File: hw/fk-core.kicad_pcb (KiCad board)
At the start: 2 copper layers, 98.8 x 37 mm, 110 parts, among them J1 RF-SMA-EDGE, J10 S2B-PH-SM4-TB, J11 RF-SMA-EDGE, J4 Conn_01x01, J5 Conn_01x03, J6 Conn_01x05, J7 CONN-HDR-2x5, J9 MICRO-USB, M1 MOUNT_HOLE, M3 MOUNT_HOLE, M4 MOUNT_HOLE, M6 MOUNT_HOLE, M7 MICROSD, Q1 2N7002LT1G, Q2 2N7002LT1G, Q3 2N7002LT1G, Q4 2N7002LT1G, SW1 SPNO, SW2 SPNO, U1 ATWINC1500-MR210PA, U10 FGPMMOPA6H, U11 MAX1704XX, U2 ATSAMD21G18A-AU, U3 RFM95W, U4 24AA02E64, U5 S25FL116K0XMFI041, U6 BQ24074RGTT, U7 PCF8523, U8 MCP1700T-3302E/MB, U9 ISL8541x, Y1 FC-135, Y2 FC-135

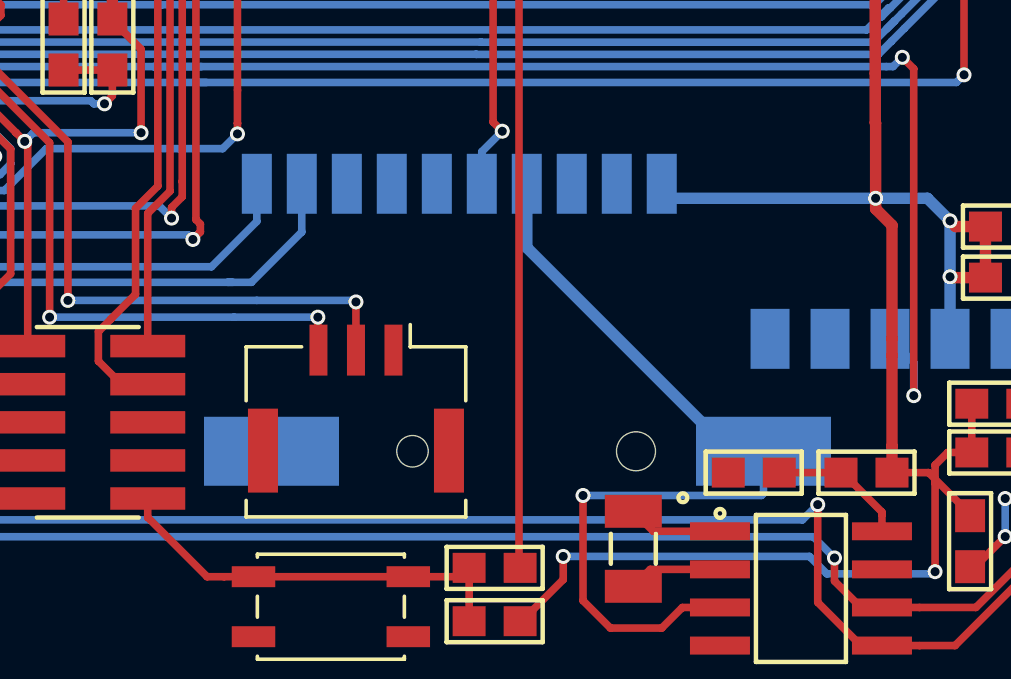
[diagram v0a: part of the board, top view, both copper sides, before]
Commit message: Nudge the coincell away from LoRa.
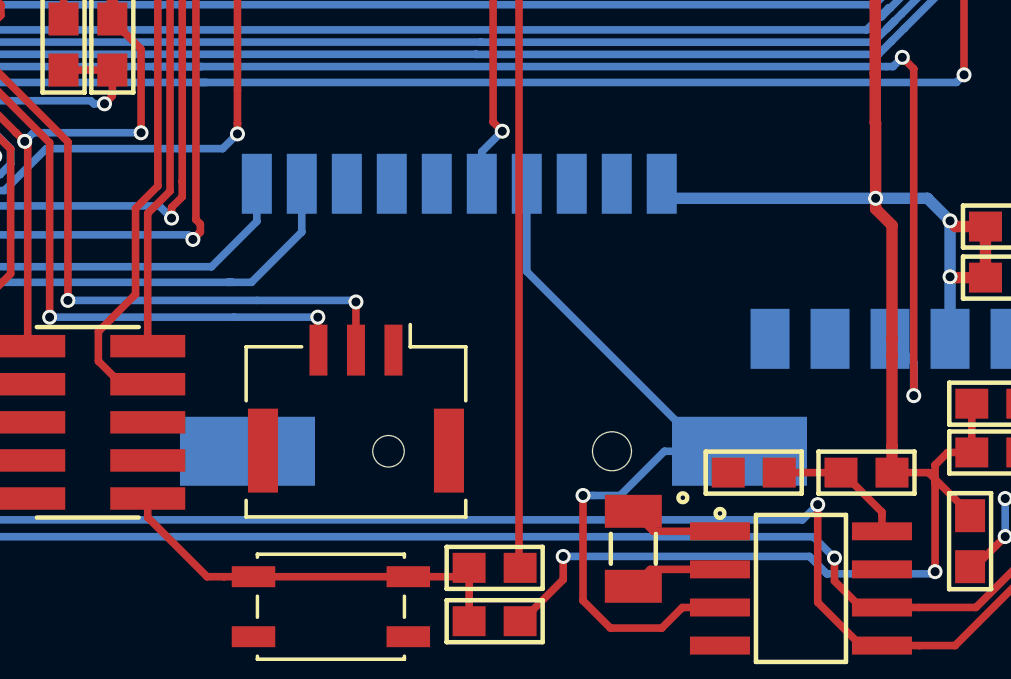
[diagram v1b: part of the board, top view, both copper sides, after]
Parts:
- moved BT1 0.80 mm to (146.3, 139.1)
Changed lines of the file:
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@@
     (links 291)
     (no_connects 0)
-    (area 62.463333 95.834285 186.108401 151.864743)
+    (area 77.293399 109.703799 176.23908 146.887001)
     (thickness 1.6)
     (drawings 23)
-    (tracks 1364)
+    (tracks 1366)
     (zones 0)
     (modules 110)
@@
   )
   (module conservify:BAT_CR1210 (layer B.Cu)
-    (at 147.1168 139.0904 270)
+    (at 146.3168 139.0904 270)
     (fp_text reference BT1 (at 0.15 -12.45 270) (layer B.SilkS) hide
       (effects (font (size 1.5 1.5) (thickness 0.15)) (justify mirror))
@@
   (segment (start 153.3652 114.62) (end 153.3652 113.8768) (width 0.254) (layer F.Cu) (net 32))
   (segment (start 153.3652 113.8768) (end 154.3812 112.8608) (width 0.254) (layer F.Cu) (net 32))
-  (segment (start 149.3012 140.5636) (end 155.2476 140.5636) (width 0.254) (layer B.Cu) (net 34))
-  (segment (start 155.2476 140.5636) (end 155.3168 140.4944) (width 0.254) (layer B.Cu) (net 34))
-  (segment (start 155.3168 140.4944) (end 155.3168 139.0904) (width 0.254) (layer B.Cu) (net 34))
+  (segment (start 147.42668 130.175) (end 147.42668 133.10028) (width 0.254) (layer B.Cu) (net 34))
+  (segment (start 147.42668 133.10028) (end 153.4168 139.0904) (width 0.254) (layer B.Cu) (net 34))
+  (segment (start 153.4168 139.0904) (end 154.5168 139.0904) (width 0.254) (layer B.Cu) (net 34))
+  (segment (start 154.5168 139.0904) (end 152.0128 139.0904) (width 0.254) (layer B.Cu) (net 34))
+  (segment (start 152.0128 139.0904) (end 150.5396 140.5636) (width 0.254) (layer B.Cu) (net 34))
+  (segment (start 150.5396 140.5636) (end 149.654753 140.5636) (width 0.254) (layer B.Cu) (net 34))
+  (segment (start 149.654753 140.5636) (end 149.3012 140.5636) (width 0.254) (layer B.Cu) (net 34))
   (segment (start 151.9258 144.9832) (end 150.213878 144.9832) (width 0.254) (layer F.Cu) (net 34))
   (segment (start 150.213878 144.9832) (end 149.3012 144.070522) (width 0.254) (layer F.Cu) (net 34))
@@
   (segment (start 153.8656 144.2974) (end 152.6116 144.2974) (width 0.254) (layer F.Cu) (net 34))
   (segment (start 152.6116 144.2974) (end 151.9258 144.9832) (width 0.254) (layer F.Cu) (net 34))
-  (segment (start 147.42668 130.6576) (end 147.42668 132.30028) (width 0.381) (layer B.Cu) (net 34))
-  (segment (start 147.42668 132.30028) (end 154.2168 139.0904) (width 0.381) (layer B.Cu) (net 34))
   (segment (start 155.436 139.0904) (end 156.536 139.0904) (width 0.381) (layer B.Cu) (net 34))
   (segment (start 122.102917 117.073717) (end 122.102917 114.946877) (width 0.254) (layer F.Cu) (net 35))
@@
     (connect_pads (clearance 0.2032))
     (min_thickness 0.2032)
-    (fill (arc_segments 32) (thermal_gap 0.254) (thermal_bridge_width 0.254))
+    (fill yes (arc_segments 32) (thermal_gap 0.254) (thermal_bridge_width 0.254))
     (polygon
       (pts
@@
     (connect_pads (clearance 0.2032))
     (min_thickness 0.2032)
-    (fill (arc_segments 32) (thermal_gap 0.254) (thermal_bridge_width 0.254))
+    (fill yes (arc_segments 32) (thermal_gap 0.254) (thermal_bridge_width 0.254))
     (polygon
       (pts
@@
     (connect_pads (clearance 0.2032))
     (min_thickness 0.2032)
-    (fill (arc_segments 32) (thermal_gap 0.254) (thermal_bridge_width 0.254))
+    (fill yes (arc_segments 32) (thermal_gap 0.254) (thermal_bridge_width 0.254))
     (polygon
       (pts
@@
     (connect_pads (clearance 0.2032))
     (min_thickness 0.2032)
-    (fill (arc_segments 32) (thermal_gap 0.254) (thermal_bridge_width 0.254))
+    (fill yes (arc_segments 32) (thermal_gap 0.254) (thermal_bridge_width 0.254))
     (polygon
       (pts
@@
     (connect_pads (clearance 0.2032))
     (min_thickness 0.2032)
-    (fill (arc_segments 32) (thermal_gap 0.254) (thermal_bridge_width 0.254))
+    (fill yes (arc_segments 32) (thermal_gap 0.254) (thermal_bridge_width 0.254))
     (polygon
       (pts
@@
     (connect_pads (clearance 0.2032))
     (min_thickness 0.2032)
-    (fill (arc_segments 32) (thermal_gap 0.254) (thermal_bridge_width 0.254))
+    (fill yes (arc_segments 32) (thermal_gap 0.254) (thermal_bridge_width 0.254))
     (polygon
       (pts
@@
     (connect_pads (clearance 0.2032))
     (min_thickness 0.2032)
-    (fill (arc_segments 32) (thermal_gap 0.254) (thermal_bridge_width 0.254))
+    (fill yes (arc_segments 32) (thermal_gap 0.254) (thermal_bridge_width 0.254))
     (polygon
       (pts
@@
     (connect_pads (clearance 0.2032))
     (min_thickness 0.2032)
-    (fill (arc_segments 32) (thermal_gap 0.254) (thermal_bridge_width 0.254))
+    (fill yes (arc_segments 32) (thermal_gap 0.254) (thermal_bridge_width 0.254))
     (polygon
       (pts

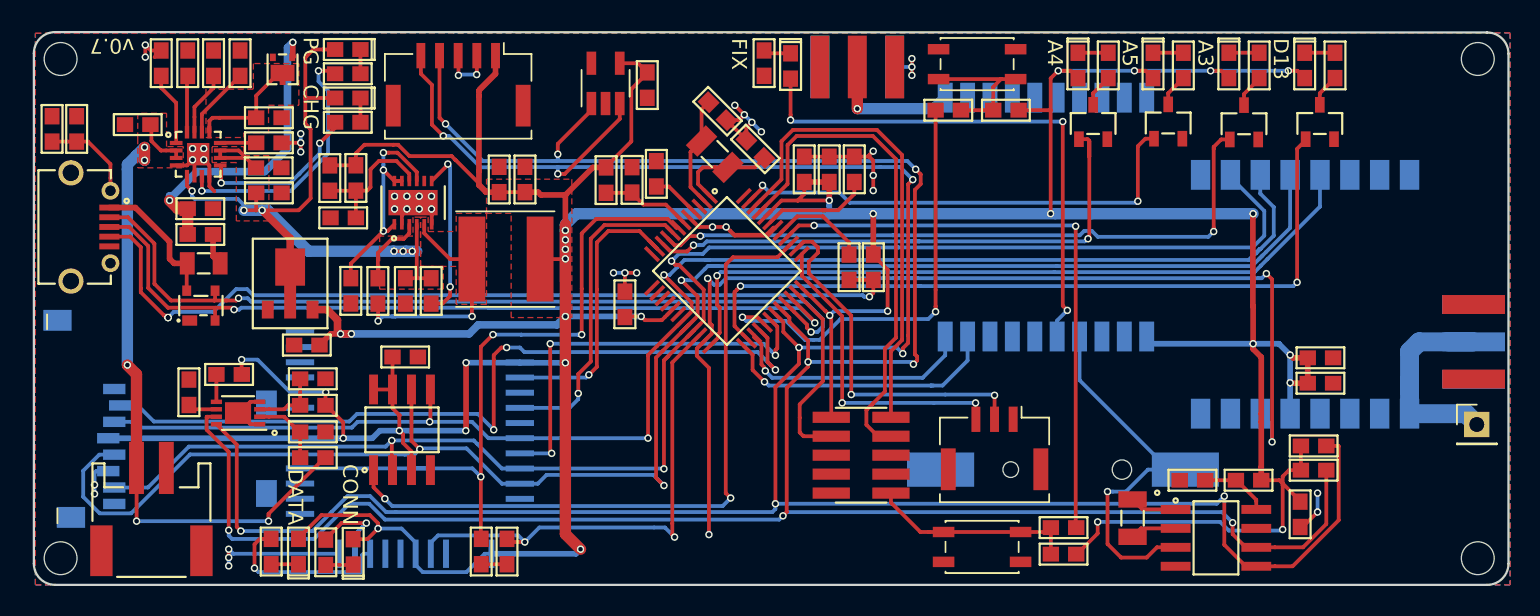
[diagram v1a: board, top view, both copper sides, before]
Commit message: Adding NFET for peripherals.
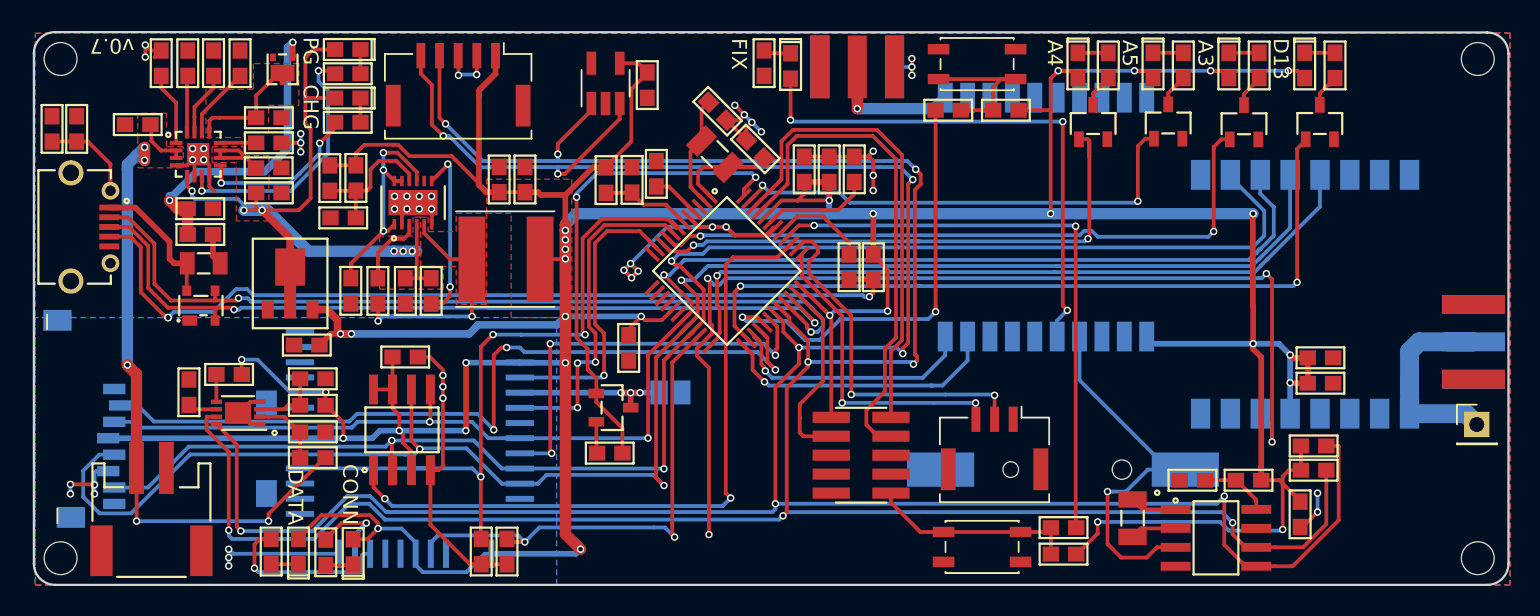
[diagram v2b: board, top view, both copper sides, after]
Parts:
- added J2: Conn_01x02, conservify:SJ_OPEN, B.Cu at (120.0, 133.9)
- added Q5: 2N7002LT1G, RocketScreamKicadLibrary:SOT-23, F.Cu at (116.2, 134.9)
- added R6: 10K, RocketScreamKicadLibrary:RES-0603, F.Cu at (116.0, 138.0)
- moved C5 2.93 mm to (117.2, 130.9), turned to 270 degrees
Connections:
- C18 pad 2: GND -> /PERIPH_GND
- M7 pad 6: GND -> /PERIPH_GND
- M7 pad MT1: GND -> /PERIPH_GND
- M7 pad MT2: GND -> /PERIPH_GND
- R1 pad 2: GND -> /PERIPH_GND
- R2 pad 2: GND -> /PERIPH_GND
- U1 pad 12: GND -> /PERIPH_GND
- U1 pad 28: GND -> /PERIPH_GND
- U1 pad 9: GND -> /PERIPH_GND
- U2 pad 48: Net-(U2-Pad48) -> /PERIPH_EN
- U5 pad 4: GND -> /PERIPH_GND
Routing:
- net /PERIPH_GND: track 0.00 -> 44.5 mm, vias 0 -> 13
- net /PERIPH_EN: track 0.00 -> 32.9 mm, vias 0 -> 2
- net GND: track 84.8 -> 82.7 mm, vias 41 -> 37
- net /WIFI_IRQ: track 22.1 -> 23.5 mm, vias 1 -> 3
- net /WIFI_WAKE: track 19.4 -> 20.6 mm
- added copper zone on B.Cu, net /PERIPH_GND

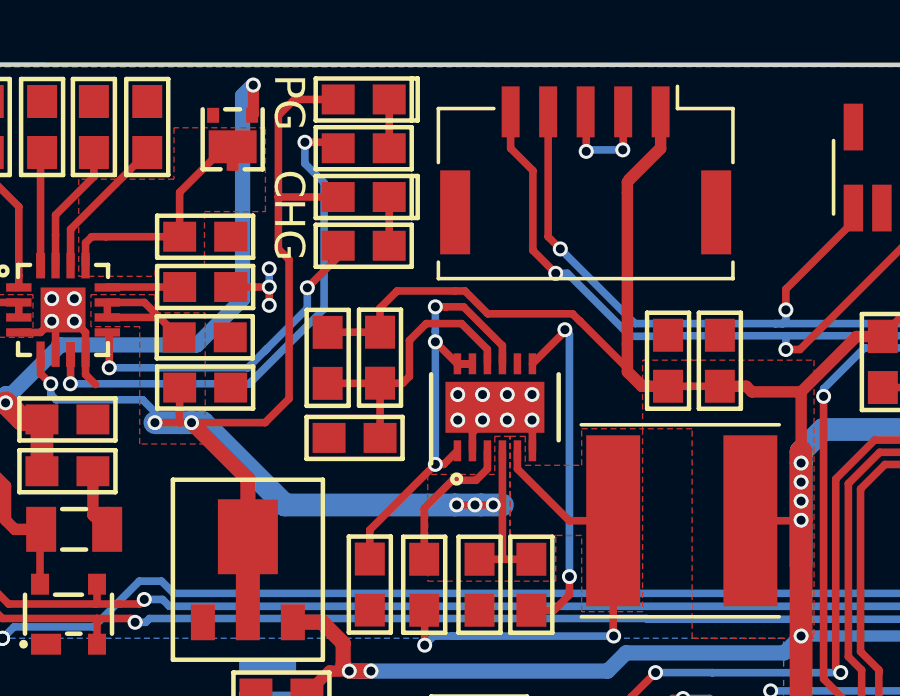
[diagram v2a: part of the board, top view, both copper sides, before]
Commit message: Expose Vbus on the module connector.
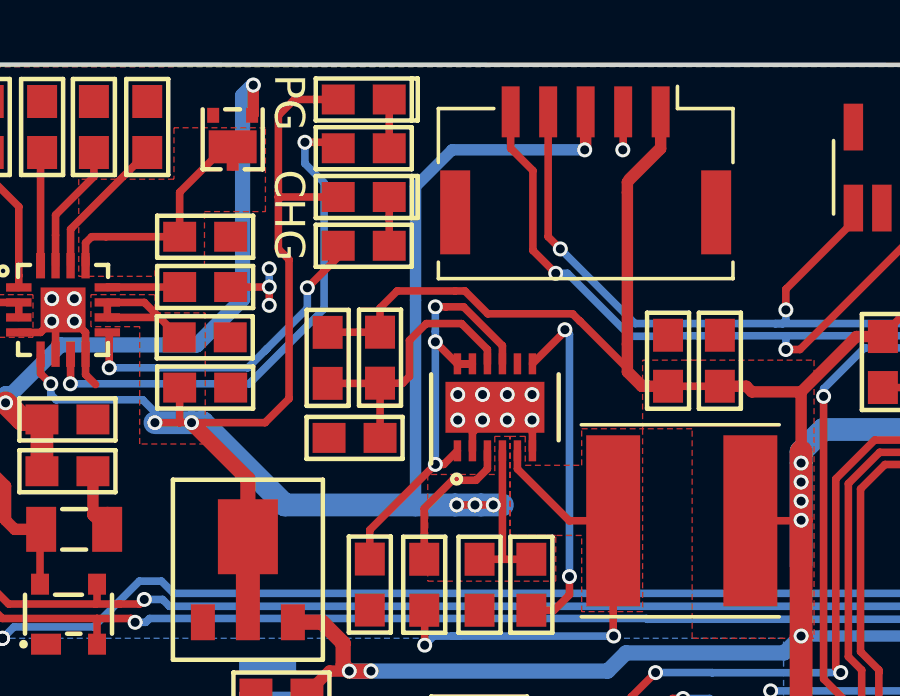
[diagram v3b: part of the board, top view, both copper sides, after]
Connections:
- J6 pad 3: GND -> VBUS
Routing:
- net VBUS: track 57.2 -> 75.3 mm, vias 6 -> 7
- net GND: track 82.7 -> 80.1 mm, vias 37 -> 36
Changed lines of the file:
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@@
     (thickness 1.6)
     (drawings 23)
-    (tracks 1428)
+    (tracks 1432)
     (zones 0)
     (modules 113)
@@
   )
   (setup
-    (last_trace_width 0.254)
+    (last_trace_width 0.381)
     (user_trace_width 0.2032)
     (user_trace_width 0.254)
@@
       (net 1 GND))
     (pad 3 smd rect (at 0 1.95 180) (size 0.6 1.7) (layers F.Cu F.Paste F.Mask)
-      (net 1 GND))
+      (net 42 VBUS))
     (pad 4 smd rect (at 1.25 1.95 180) (size 0.6 1.7) (layers F.Cu F.Paste F.Mask)
       (net 7 /SCL))
@@
   (segment (start 135.0372 112.1156) (end 136.1948 112.1156) (width 0.254) (layer B.Cu) (net 1))
   (via (at 136.1948 112.1156) (size 0.5) (drill 0.3) (layers F.Cu B.Cu) (net 1))
-  (segment (start 105.8164 112.6744) (end 105.8164 111.3752) (width 0.254) (layer F.Cu) (net 1))
-  (segment (start 105.8164 111.3752) (end 105.7976 111.3564) (width 0.254) (layer F.Cu) (net 1))
-  (segment (start 107.0356 112.6236) (end 105.8672 112.6236) (width 0.254) (layer B.Cu) (net 1))
-  (segment (start 105.8672 112.6236) (end 105.8164 112.6744) (width 0.254) (layer B.Cu) (net 1))
-  (via (at 105.8164 112.6744) (size 0.5) (drill 0.3) (layers F.Cu B.Cu) (net 1))
   (segment (start 107.0476 111.3564) (end 107.0476 112.6116) (width 0.254) (layer F.Cu) (net 1))
   (segment (start 107.0476 112.6116) (end 107.0356 112.6236) (width 0.254) (layer F.Cu) (net 1))
-  (via (at 107.0356 112.6236) (size 0.5) (drill 0.3) (layers F.Cu B.Cu) (net 1))
   (via (at 123.7488 122.8344) (size 0.5) (drill 0.3) (layers F.Cu B.Cu) (net 1))
   (via (at 122.8344 122.8344) (size 0.5) (drill 0.3) (layers F.Cu B.Cu) (net 1))
@@
   (segment (start 91.87219 134.549214) (end 91.48469 134.936714) (width 0.254) (layer F.Cu) (net 1))
   (segment (start 102.244819 127.970777) (end 102.244819 127.920777) (width 0.254) (layer F.Cu) (net 1))
+  (via (at 107.0356 112.6236) (size 0.5) (drill 0.3) (layers F.Cu B.Cu) (net 1))
   (segment (start 117.221 130.087) (end 117.221 129.667) (width 0.254) (layer F.Cu) (net 2))
   (segment (start 117.221 129.667) (end 118.0592 128.8288) (width 0.254) (layer F.Cu) (net 2))
@@
   (via (at 93.091 142.5448) (size 0.5) (drill 0.3) (layers F.Cu B.Cu) (net 41))
   (via (at 84.2518 142.5448) (size 0.5) (drill 0.3) (layers F.Cu B.Cu) (net 41))
+  (segment (start 105.7656 112.6236) (end 101.346 112.6236) (width 0.381) (layer B.Cu) (net 42))
+  (segment (start 101.346 112.6236) (end 100.1268 113.8428) (width 0.381) (layer B.Cu) (net 42))
+  (segment (start 100.1268 117.638906) (end 100.1268 113.8428) (width 0.381) (layer B.Cu) (net 42))
+  (segment (start 101.4476 124.46) (end 100.1268 124.46) (width 0.762) (layer B.Cu) (net 42))
+  (segment (start 100.1268 117.638906) (end 100.1268 124.46) (width 0.381) (layer B.Cu) (net 42))
+  (segment (start 100.1268 124.46) (end 95.769647 124.46) (width 0.762) (layer B.Cu) (net 42))
+  (segment (start 105.7976 111.3564) (end 105.7976 112.5916) (width 0.381) (layer F.Cu) (net 42))
+  (segment (start 105.7976 112.5916) (end 105.7656 112.6236) (width 0.381) (layer F.Cu) (net 42))
+  (via (at 105.7656 112.6236) (size 0.5) (drill 0.3) (layers F.Cu B.Cu) (net 42))
+  (segment (start 105.8164 111.3752) (end 105.7976 111.3564) (width 0.254) (layer F.Cu) (net 42))
   (segment (start 95.5548 115.9256) (end 95.5548 114.1984) (width 0.254) (layer F.Cu) (net 42))
   (segment (start 95.5548 114.1984) (end 95.5548 113.9952) (width 0.254) (layer F.Cu) (net 42))
@@
   (segment (start 102.3112 124.46) (end 101.4476 124.46) (width 0.762) (layer B.Cu) (net 42))
   (via (at 101.4984 124.46) (size 0.5) (drill 0.3) (layers F.Cu B.Cu) (net 42))
-  (segment (start 101.4476 124.46) (end 95.769647 124.46) (width 0.762) (layer B.Cu) (net 42))
   (segment (start 102.3112 124.46) (end 101.4476 124.46) (width 0.254) (layer F.Cu) (net 42))
   (segment (start 103.022819 124.46) (end 102.3112 124.46) (width 0.762) (layer B.Cu) (net 42))
@@
     (connect_pads (clearance 0.2032))
     (min_thickness 0.2032)
-    (fill yes (arc_segments 32) (thermal_gap 0.254) (thermal_bridge_width 0.254))
+    (fill (arc_segments 32) (thermal_gap 0.254) (thermal_bridge_width 0.254))
     (polygon
       (pts
@@
     (connect_pads (clearance 0.2032))
     (min_thickness 0.2032)
-    (fill yes (arc_segments 32) (thermal_gap 0.254) (thermal_bridge_width 0.254))
+    (fill (arc_segments 32) (thermal_gap 0.254) (thermal_bridge_width 0.254))
     (polygon
       (pts
@@
     (connect_pads (clearance 0.2032))
     (min_thickness 0.2032)
-    (fill yes (arc_segments 32) (thermal_gap 0.254) (thermal_bridge_width 0.254))
+    (fill (arc_segments 32) (thermal_gap 0.254) (thermal_bridge_width 0.254))
     (polygon
       (pts
@@
     (connect_pads (clearance 0.2032))
     (min_thickness 0.2032)
-    (fill yes (arc_segments 32) (thermal_gap 0.254) (thermal_bridge_width 0.254))
+    (fill (arc_segments 32) (thermal_gap 0.254) (thermal_bridge_width 0.254))
     (polygon
       (pts
@@
     (connect_pads (clearance 0.2032))
     (min_thickness 0.2032)
-    (fill yes (arc_segments 32) (thermal_gap 0.254) (thermal_bridge_width 0.254))
+    (fill (arc_segments 32) (thermal_gap 0.254) (thermal_bridge_width 0.254))
     (polygon
       (pts
@@
     (connect_pads (clearance 0.2032))
     (min_thickness 0.2032)
-    (fill yes (arc_segments 32) (thermal_gap 0.254) (thermal_bridge_width 0.254))
+    (fill (arc_segments 32) (thermal_gap 0.254) (thermal_bridge_width 0.254))
     (polygon
       (pts
@@
     (connect_pads (clearance 0.2032))
     (min_thickness 0.2032)
-    (fill yes (arc_segments 32) (thermal_gap 0.254) (thermal_bridge_width 0.254))
+    (fill (arc_segments 32) (thermal_gap 0.254) (thermal_bridge_width 0.254))
     (polygon
       (pts
@@
     (connect_pads (clearance 0.2032))
     (min_thickness 0.2032)
-    (fill yes (arc_segments 32) (thermal_gap 0.254) (thermal_bridge_width 0.254))
+    (fill (arc_segments 32) (thermal_gap 0.254) (thermal_bridge_width 0.254))
     (polygon
       (pts
@@
     (connect_pads (clearance 0.2032))
     (min_thickness 0.254)
-    (fill yes (arc_segments 16) (thermal_gap 0.508) (thermal_bridge_width 0.508))
+    (fill (arc_segments 16) (thermal_gap 0.508) (thermal_bridge_width 0.508))
     (polygon
       (pts
